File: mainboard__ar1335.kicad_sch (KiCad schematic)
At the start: 28 parts

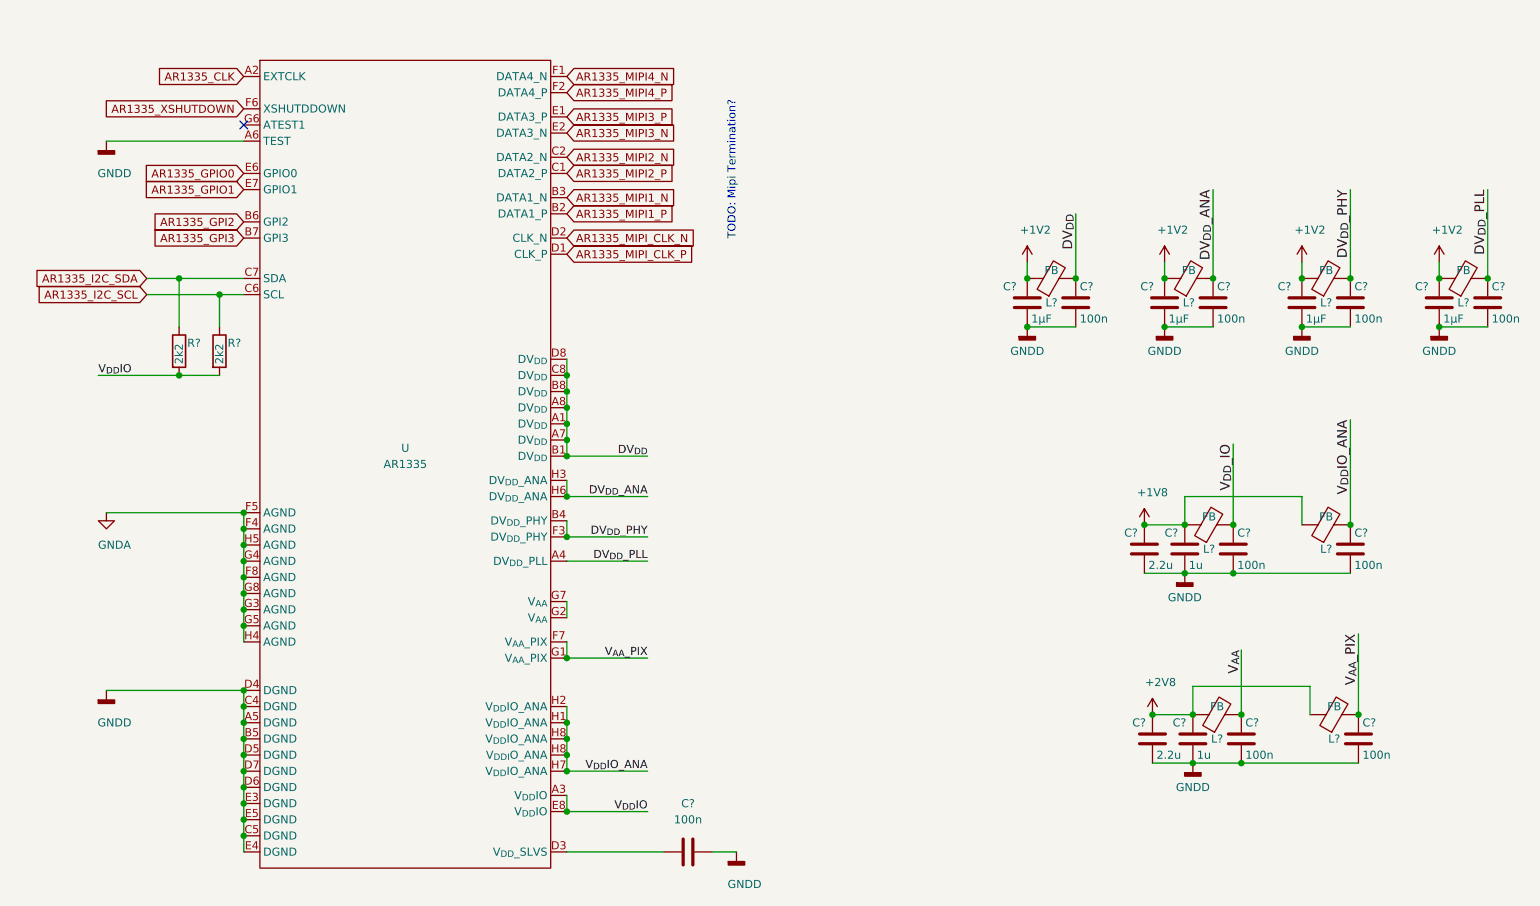
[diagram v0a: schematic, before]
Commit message: small tweaks; add mipi termination
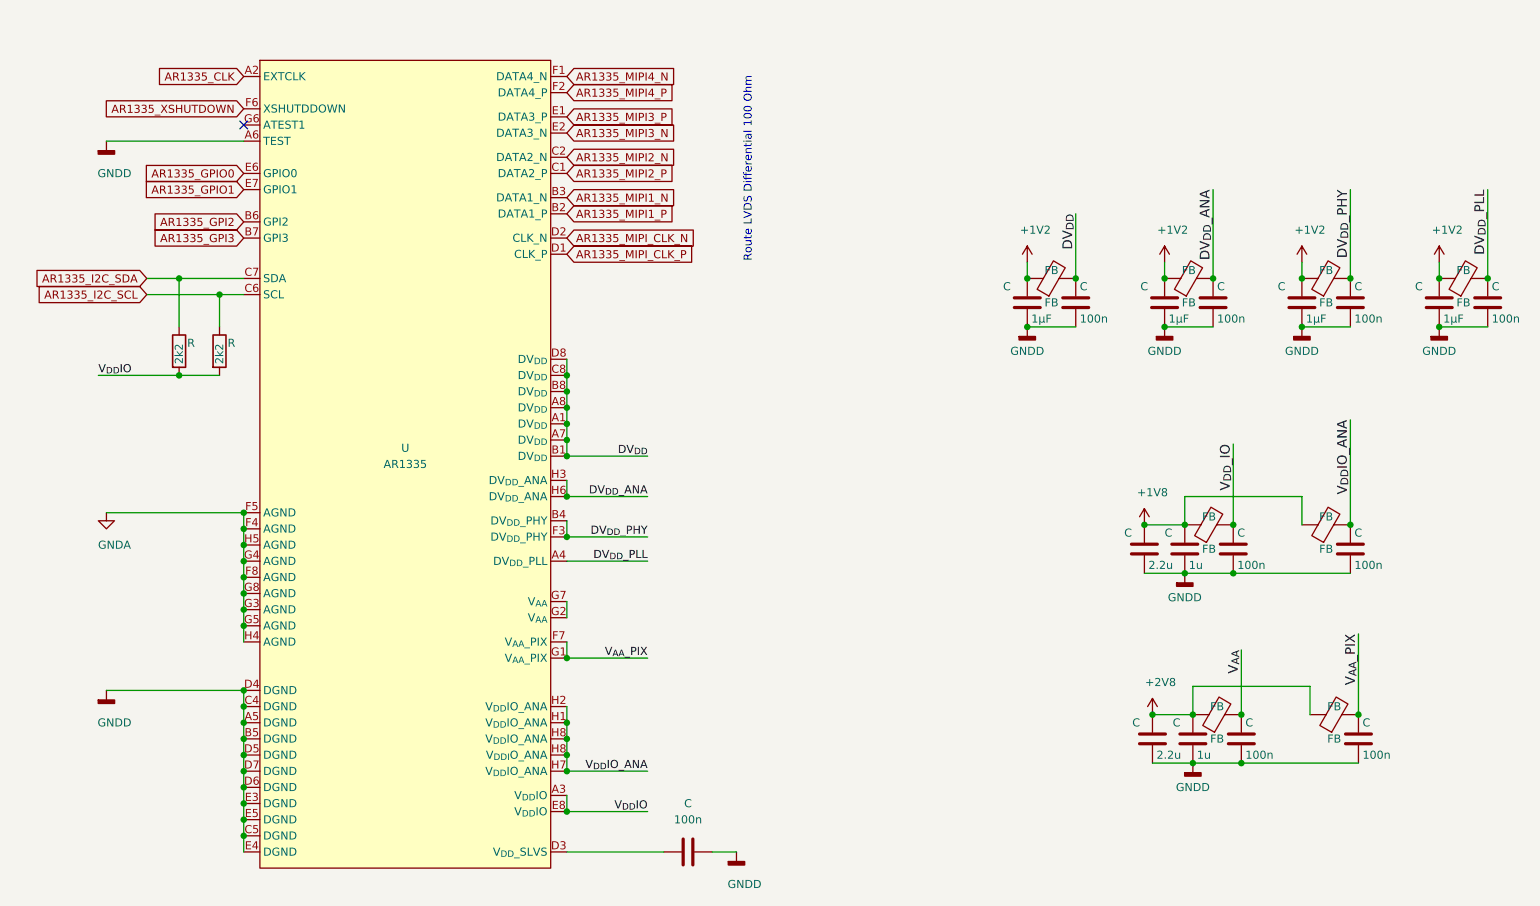
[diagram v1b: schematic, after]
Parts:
- U: symbol parts:AR1335 -> image_sensor:AR1335
- gave numbers to parts that had none: 3
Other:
- note added: "Route LVDS Differential 100 Ohm"
- note removed: "TODO: Mipi Termination?"
